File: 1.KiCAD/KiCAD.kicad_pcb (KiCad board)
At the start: 2 copper layers, 20 parts, among them J1 Conn_02x20_Odd_Even, J10 CELL_1, J11 CELL_2, J12 CELL_3, J13 CELL_4, J2 Conn_02x20_Odd_Even, J3 TEMP, J4 TEMP, J5 BAT+, J6 BAT-, J7 LOAD+, J8 LOAD-, Q1 Charge, Q2 Discharge, Q3 Charge, Q4 Discharge, U1 MUX, U2 MUX

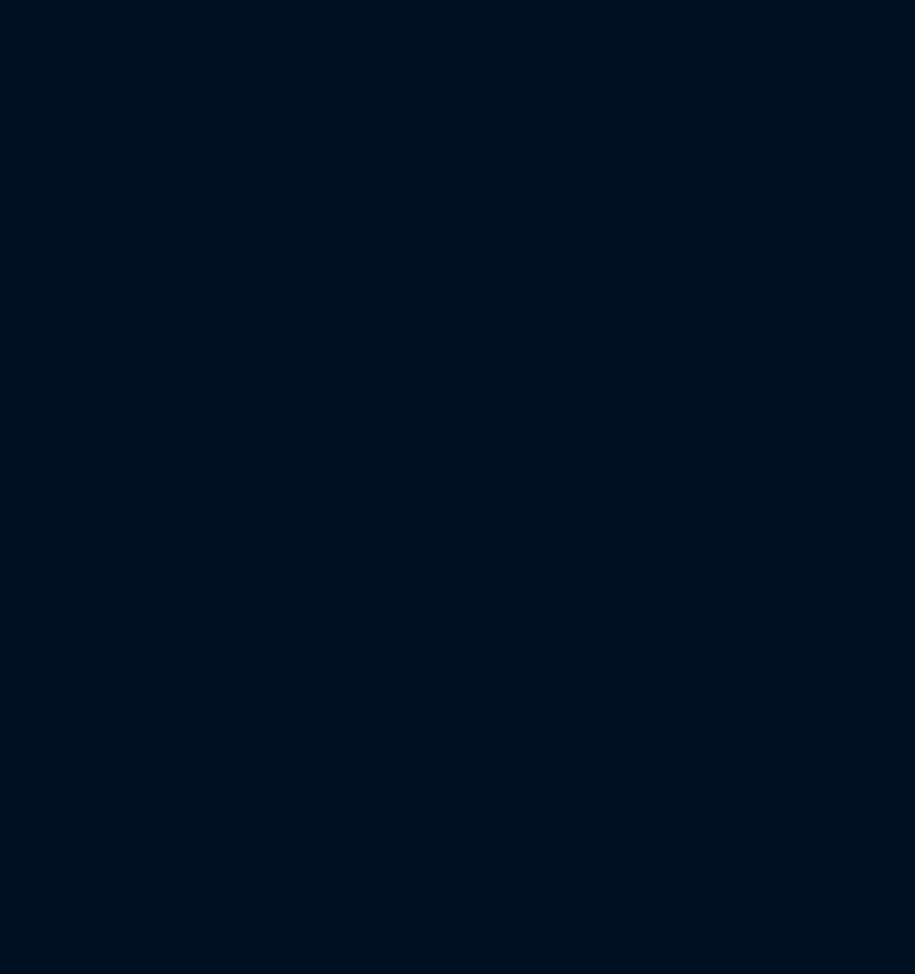
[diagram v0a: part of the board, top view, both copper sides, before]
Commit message: BOM finished
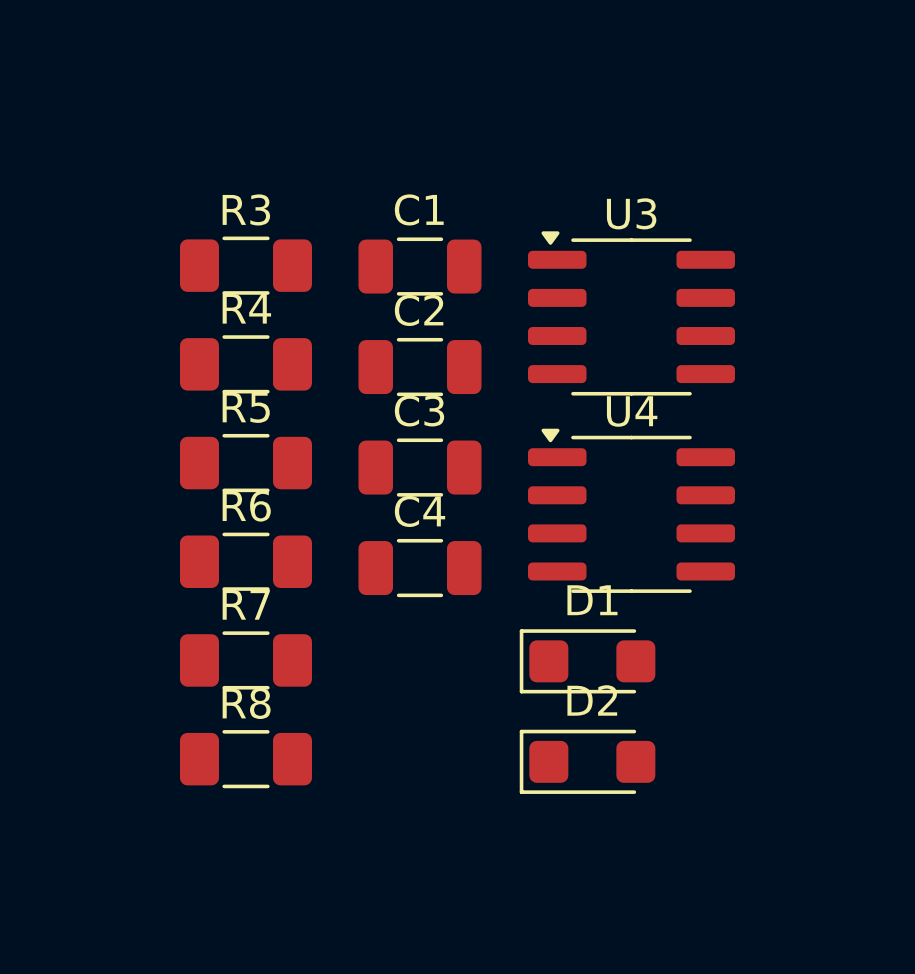
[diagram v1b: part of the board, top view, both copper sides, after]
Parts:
- added C1: 100NF_50V_CER, VAMK_C_SMD:C1206, F.Cu at (145.3, 146.5)
- added C2: 100NF_50V_CER, VAMK_C_SMD:C1206, F.Cu at (145.3, 149.8)
- added C3: 100NF_50V_CER, VAMK_C_SMD:C1206, F.Cu at (145.3, 153.2)
- added C4: 100NF_50V_CER, VAMK_C_SMD:C1206, F.Cu at (145.3, 156.5)
- added D1: 3.3V, Diode_SMD:D_SMF, F.Cu at (151.1, 159.7)
- added D2: 3.3V, Diode_SMD:D_SMF, F.Cu at (151.1, 163.0)
- added R3: 10k, VAMK_R_SMD:1206, F.Cu at (139.5, 146.5)
- added R4: 10k, VAMK_R_SMD:1206, F.Cu at (139.5, 149.8)
- added R5: 1m, VAMK_R_SMD:1206, F.Cu at (139.5, 153.0)
- added R6: 160R, VAMK_R_SMD:1206, F.Cu at (139.5, 156.3)
- added R7: 10k, VAMK_R_SMD:1206, F.Cu at (139.5, 159.6)
- added R8: 10k, VAMK_R_SMD:1206, F.Cu at (139.5, 162.9)
- added U3: AD8021AR, Package_SO:SOIC-8_3.9x4.9mm_P1.27mm, F.Cu at (152.4, 148.2)
- added U4: AD8021AR, Package_SO:SOIC-8_3.9x4.9mm_P1.27mm, F.Cu at (152.4, 154.8)
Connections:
- J1 pad 16: unconnected-(J1-Pin_16-Pad16) -> 3.3V
- J1 pad 28: unconnected-(J1-Pin_28-Pad28) -> PA0
- J1 pad 30: unconnected-(J1-Pin_30-Pad30) -> PA1
- J1 pad 32: unconnected-(J1-Pin_32-Pad32) -> PA4
- J10 pad 1: unconnected-(J10-Pin_1-Pad1) -> C1-
- J10 pad 2: unconnected-(J10-Pin_2-Pad2) -> C1+
- J11 pad 1: unconnected-(J11-Pin_1-Pad1) -> C2-
- J11 pad 2: unconnected-(J11-Pin_2-Pad2) -> C2+
- J12 pad 1: unconnected-(J12-Pin_1-Pad1) -> C3-
- J12 pad 2: unconnected-(J12-Pin_2-Pad2) -> C3+
- J13 pad 1: unconnected-(J13-Pin_1-Pad1) -> C4-
- J13 pad 2: unconnected-(J13-Pin_2-Pad2) -> C4+
- J2 pad 16: unconnected-(J2-Pin_16-Pad16) -> PC1
- J2 pad 17: unconnected-(J2-Pin_17-Pad17) -> PB0
- J2 pad 18: unconnected-(J2-Pin_18-Pad18) -> PC0
- J3 pad 2: ADC_1 -> PC0
- J4 pad 2: ADC_1 -> PC1
- J6 pad 1: unconnected-(J6-Pin_1-Pad1) -> BAT-
- J7 pad 1: unconnected-(J7-Pin_1-Pad1) -> BAT+
- J8 pad 1: unconnected-(J8-Pin_1-Pad1) -> LOAD-
- Q1 pad 1: unconnected-(Q1-S-Pad1) -> LOAD-
- Q1 pad 4: unconnected-(Q1-G-Pad4) -> PA1
- Q1 pad 8: unconnected-(Q1-D-Pad8) -> Net-(Q1-D)
- Q2 pad 1: BAT+ -> Net-(Q2-S)
- Q2 pad 4: unconnected-(Q2-G-Pad4) -> PA0
- Q2 pad 8: unconnected-(Q2-D-Pad8) -> Net-(Q1-D)
- Q3 pad 1: unconnected-(Q3-S-Pad1) -> LOAD-
- Q3 pad 4: unconnected-(Q3-G-Pad4) -> PA1
- Q3 pad 8: unconnected-(Q3-D-Pad8) -> Net-(Q1-D)
- Q4 pad 1: unconnected-(Q4-S-Pad1) -> Net-(Q2-S)
- Q4 pad 4: unconnected-(Q4-G-Pad4) -> PA0
- Q4 pad 8: unconnected-(Q4-D-Pad8) -> Net-(Q1-D)
- R1 pad 2: ADC_1 -> PC0
- R2 pad 2: ADC_1 -> PC1

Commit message: Schematic and PCB V1 done
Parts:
- moved J11 121.3 mm to (131.5, 53.2), turned to 90 degrees
- moved J8 116.3 mm to (176.0, 62.0)
- moved J10 111.2 mm to (121.8, 53.5), turned to 90 degrees
- moved U1 103.2 mm to (152.6, 93.6)
- moved J6 101.8 mm to (114.8, 61.2)
- moved U2 101.3 mm to (144.8, 93.8), turned to 90 degrees
- moved R5 94.5 mm to (138.2, 58.5)
- moved R6 91.2 mm to (135.5, 65.2), turned to -90 degrees
- moved C4 90.0 mm to (118.0, 70.8), turned to 90 degrees
- moved C3 89.9 mm to (112.5, 69.5), turned to 180 degrees
- moved R4 86.4 mm to (129.0, 64.0), turned to 180 degrees
- moved Q3 85.5 mm to (162.0, 66.8), turned to 180 degrees
- moved C2 85.3 mm to (179.0, 71.5), turned to 180 degrees
- moved J12 85.2 mm to (164.8, 132.5), turned to -90 degrees
- moved Q4 84.6 mm to (149.0, 66.9)
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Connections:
- D1 pad 1: PB0 -> PB1
- J1 pad 34: unconnected-(J1-Pin_34-Pad34) -> PB1
- J1 pad 35: unconnected-(J1-Pin_35-Pad35) -> PC2
- J1 pad 37: unconnected-(J1-Pin_37-Pad37) -> PC3
- J1 pad 8: unconnected-(J1-Pin_8-Pad8) -> GND
- J2 pad 17: PB0 -> unconnected-(J2-Pin_17-Pad17)
- J3 pad 1: +3.3V -> 3.3V
- J3 pad 2: PC0 -> PA0
- J4 pad 1: +3.3V -> 3.3V
- J4 pad 2: PC1 -> PA1
- Q1 pad 4: PA1 -> PC0
- Q2 pad 4: PA0 -> PC1
- Q3 pad 4: PA1 -> PC0
- Q4 pad 4: PA0 -> PC1
- R1 pad 2: PC0 -> PA0
- R2 pad 2: PC1 -> PA1
- R6 pad 1: Net-(Q2-S) -> BAT-
- U1 pad 1: unconnected-(U1-A0-Pad1) -> PC2
- U1 pad 10: unconnected-(U1-A1-Pad10) -> PC3
- U1 pad 2: unconnected-(U1-S1-Pad2) -> C1+
- U1 pad 3: unconnected-(U1-GND-Pad3) -> GND
- U1 pad 4: unconnected-(U1-S3-Pad4) -> C3+
- U1 pad 5: unconnected-(U1-EN-Pad5) -> 3.3V
- U1 pad 6: unconnected-(U1-VDD-Pad6) -> 3.3V
- U1 pad 7: unconnected-(U1-S4-Pad7) -> C4+
- U1 pad 8: unconnected-(U1-D-Pad8) -> Net-(U1-D)
- U1 pad 9: unconnected-(U1-S2-Pad9) -> C2+
- U2 pad 1: unconnected-(U2-A0-Pad1) -> PC2
- U2 pad 10: unconnected-(U2-A1-Pad10) -> PC3
- U2 pad 2: unconnected-(U2-S1-Pad2) -> C1-
- U2 pad 3: unconnected-(U2-GND-Pad3) -> GND
- U2 pad 4: unconnected-(U2-S3-Pad4) -> C3-
- U2 pad 5: unconnected-(U2-EN-Pad5) -> 3.3V
- U2 pad 6: unconnected-(U2-VDD-Pad6) -> 3.3V
- U2 pad 7: unconnected-(U2-S4-Pad7) -> C4-
- U2 pad 8: unconnected-(U2-D-Pad8) -> Net-(U2-D)
- U2 pad 9: unconnected-(U2-S2-Pad9) -> C2-
- U3 pad 1: BAT- -> Net-(Q2-S)
- U4 pad 1: unconnected-(U4--IN-Pad1) -> Net-(U2-D)
- U4 pad 4: unconnected-(U4-+iN-Pad4) -> Net-(U1-D)
- U4 pad 6: unconnected-(U4-REF-Pad6) -> GND
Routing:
- net BAT+: track 0.00 -> 179.3 mm
- net 3.3V: track 0.00 -> 173.2 mm, vias 0 -> 2
- net PC2: track 0.00 -> 122.6 mm, vias 0 -> 4
- net PC1: track 0.00 -> 116.7 mm, vias 0 -> 2
- net PC0: track 0.00 -> 81.8 mm, vias 0 -> 2
- net PC3: track 0.00 -> 74.2 mm, vias 0 -> 4
- net C3-: track 0.00 -> 68.2 mm, vias 0 -> 2
- net Net-(C1-Pad2): track 0.00 -> 60.7 mm
- net C1-: track 0.00 -> 60.1 mm, vias 0 -> 2
- net C1+: track 0.00 -> 56.4 mm, vias 0 -> 2
- net C2+: track 0.00 -> 54.3 mm, vias 0 -> 2
- net PA1: track 0.00 -> 52.5 mm
- net C3+: track 0.00 -> 51.7 mm, vias 0 -> 2
- net C2-: track 0.00 -> 50.6 mm, vias 0 -> 2
- net C4-: track 0.00 -> 48.6 mm, vias 0 -> 2
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- added copper zone on B.Cu, net GND
- added copper zone on F.Cu, net GND
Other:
- board outline added: 80.2 x 90.5 mm
